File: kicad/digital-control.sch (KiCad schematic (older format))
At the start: 35 parts, among them J1 SWD, J2 EXTERNAL_OUT, J3 EXTERNAL_IN, J4 USB_OTG, U1 STM32F042FxP, U2 USBLC6-2

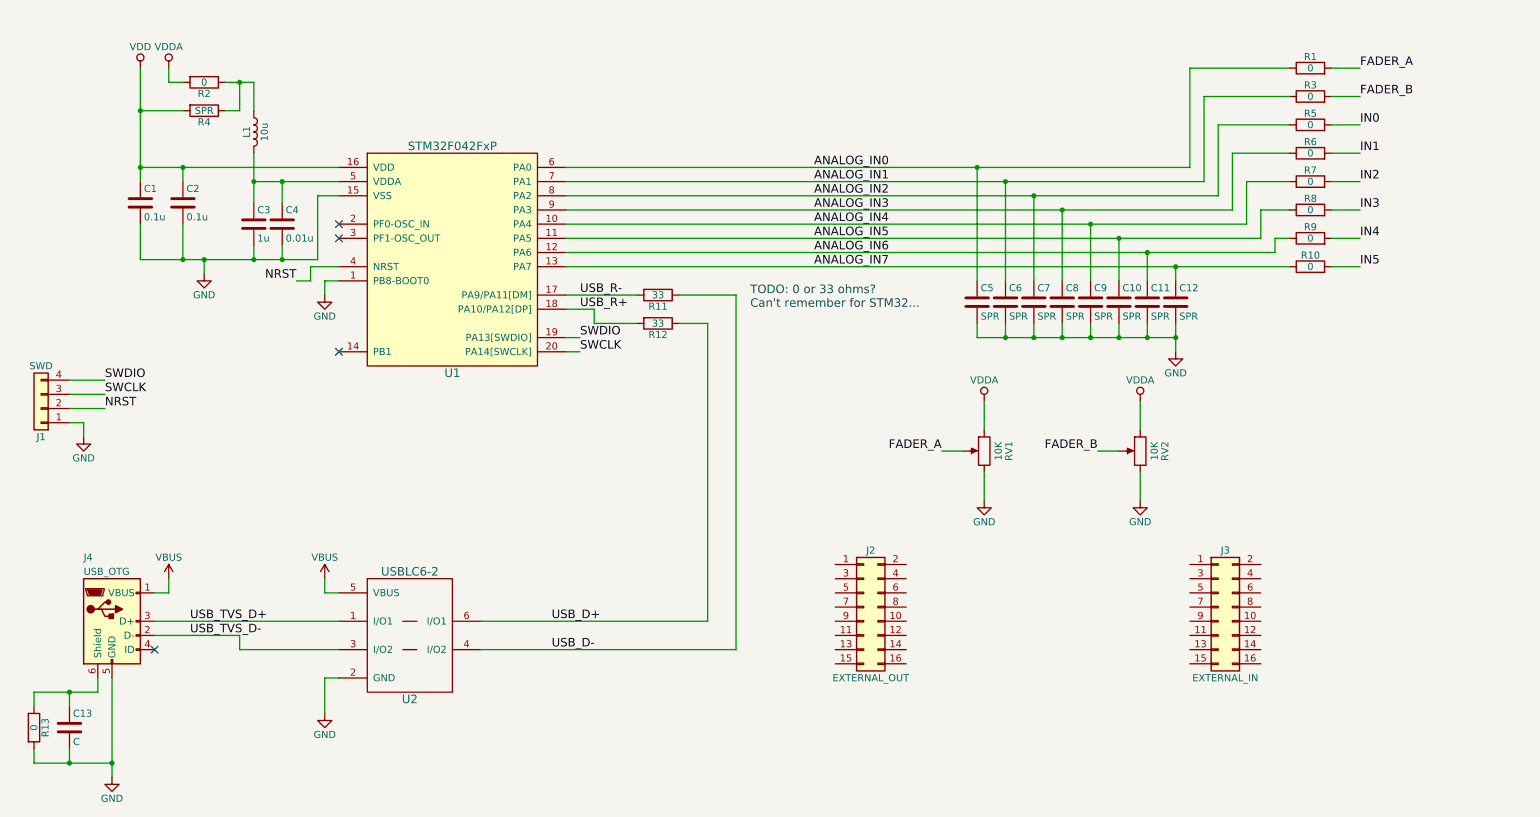
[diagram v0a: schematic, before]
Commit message: Finished initial part selection, built footprints
I'm not sure about my footprint selection for the expansion headers,
even though it is just a 0.1" header I want to be fairly exact about the
length the pins stick out and how close the female header is to the
edge, so that I can get a good distance between the two boards.
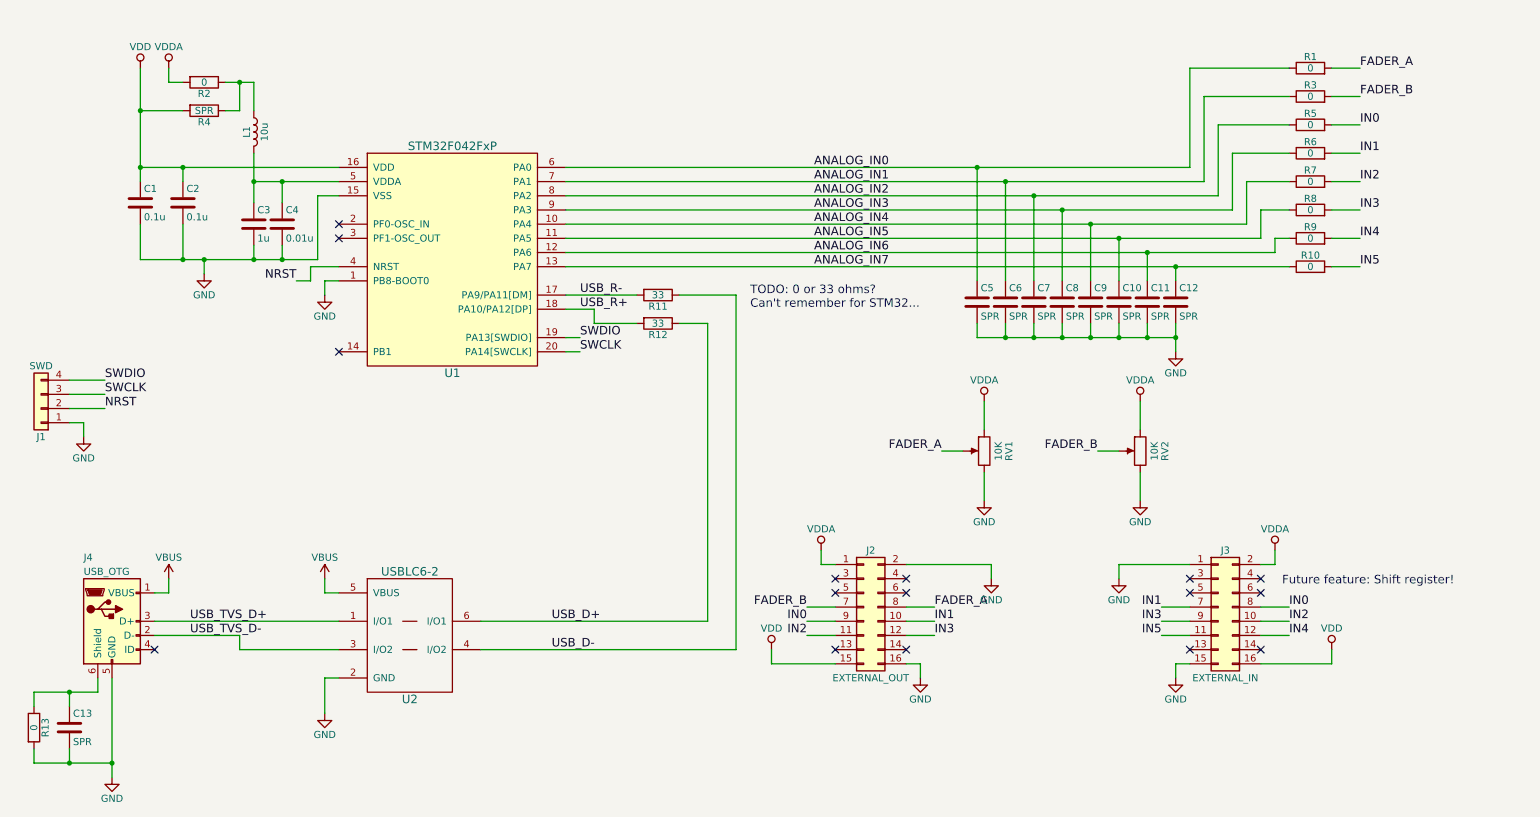
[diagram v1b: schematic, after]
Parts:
- C1, C2: footprint (none) -> Capacitors_SMD:C_0402; Part No. (none) -> 1276-1043-1-ND
- C10, C11, C12, C5, C6, C7, C8, C9: footprint (none) -> Capacitors_SMD:C_0402
- C13: value C -> SPR; footprint (none) -> Capacitors_SMD:C_0402
- C3: footprint (none) -> Capacitors_SMD:C_0603; Part No. (none) -> 1276-6524-1-ND
- C4: footprint (none) -> Capacitors_SMD:C_0402; Part No. (none) -> 399-1038-1-ND
- J1: footprint (none) -> midi-fader:JST-SH-4
- J2: footprint (none) -> Pin_Headers:Pin_Header_Angled_2x08_Pitch2.54mm
- J3: footprint (none) -> Socket_Strips:Socket_Strip_Angled_2x08_Pitch2.54mm
- J4: footprint (none) -> midi-fader:AMP-10104110-USB
- L1: footprint (none) -> Resistors_SMD:R_0805; Part No. (none) -> 587-2045-1-ND
- R1, R10, R11, R12, R13, R2, R3, R4, R5, R6, R7, R8, R9: footprint (none) -> Resistors_SMD:R_0402
- RV1, RV2: footprint (none) -> midi-fader:BOURNS_PTA60X3
- U1: footprint (none) -> Housings_SSOP:TSSOP-20_4.4x6.5mm_Pitch0.65mm
- U2: footprint (none) -> midi-fader:SOT-666
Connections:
- net FADER_A: now also J2.8 (Pin_8)
- net FADER_B: now also J2.7 (Pin_7)
- net GND: now also J2.16 (Pin_16), J2.2 (Pin_2), J3.1 (Pin_1), J3.15 (Pin_15)
- net IN0: now also J2.9 (Pin_9), J3.8 (Pin_8)
- net IN1: now also J2.10 (Pin_10), J3.7 (Pin_7)
- net IN2: now also J2.11 (Pin_11), J3.10 (Pin_10)
- net IN3: now also J2.12 (Pin_12), J3.9 (Pin_9)
- net IN4: now also J3.12 (Pin_12)
- net IN5: now also J3.11 (Pin_11)
- net VDD: now also J2.15 (Pin_15), J3.16 (Pin_16)
- net VDDA: now also J2.1 (Pin_1), J3.2 (Pin_2)
- no-connect marks 4 -> 16
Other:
- note added: "Future feature: Shift register!"

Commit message: Changed microcontroller to 32-LQFP variety
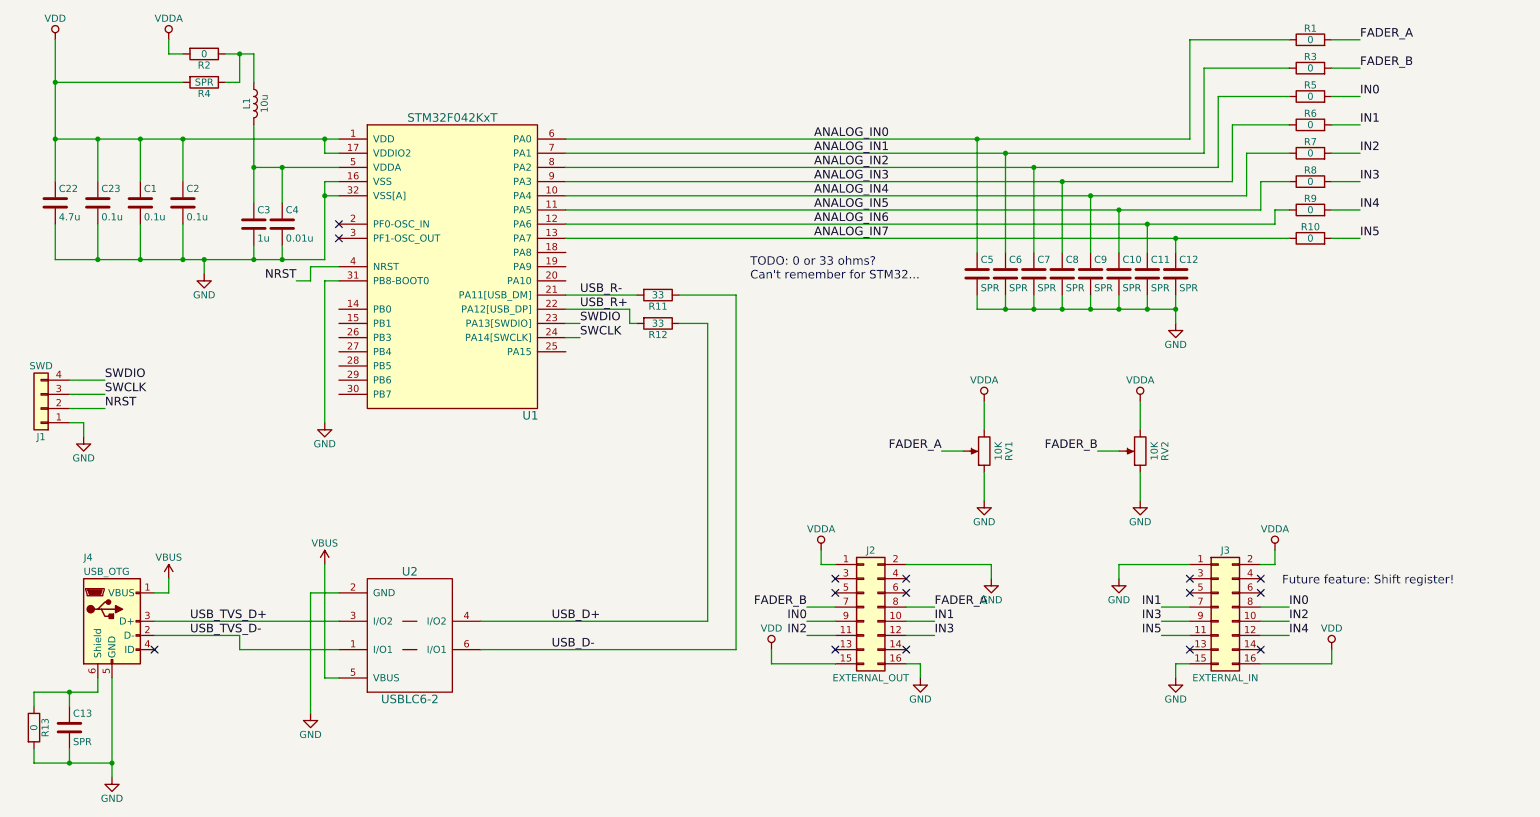
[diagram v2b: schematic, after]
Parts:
- removed U1: STM32F042FxP, Housings_SSOP:TSSOP-20_4.4x6.5mm_Pitch0.65mm, symbol STM32F042FxP
- added C22: 4.7u, Capacitors_SMD:C_0805, symbol C
- added C23: 0.1u, Capacitors_SMD:C_0402, symbol C
- added U1: STM32F042KxT, Housings_QFP:LQFP-32_7x7mm_Pitch0.8mm, symbol STM32F042KxT
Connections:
- net ANALOG_IN0: now also U1.6 (PA0)
- net ANALOG_IN1: now also U1.7 (PA1)
- net ANALOG_IN2: now also U1.8 (PA2)
- net ANALOG_IN3: now also U1.9 (PA3)
- net ANALOG_IN4: now also U1.10 (PA4)
- net ANALOG_IN5: now also U1.11 (PA5)
- net ANALOG_IN6: now also U1.12 (PA6)
- net ANALOG_IN7: now also U1.13 (PA7)
- net GND: now also RV1.1, RV2.1, C22.2, C23.2, U1.16 (VSS), U1.31 (PB8-BOOT0), U1.32 (VSS[A]); no longer RV1.3, RV2.3
- net NRST: now also U1.4 (NRST)
- net SWCLK: now also U1.24 (PA14[SWCLK])
- net SWDIO: now also U1.23 (PA13[SWDIO])
- net USB_D+: now also U2.4 (I/O2); no longer U2.6 (I/O1)
- net USB_D-: now also U2.6 (I/O1); no longer U2.4 (I/O2)
- net USB_R+: now also U1.22 (PA12[USB_DP])
- net USB_R-: now also U1.21 (PA11[USB_DM])
- net USB_TVS_D+: now also U2.3 (I/O2); no longer U2.1 (I/O1)
- net USB_TVS_D-: now also U2.1 (I/O1); no longer U2.3 (I/O2)
- net VDD: now also C22.1, C23.1, U1.1 (VDD), U1.17 (VDDIO2)
- net VDDA: now also RV1.3, RV2.3; no longer RV1.1, RV2.1
- net at C3.1, C4.1, L1.2: now also U1.5 (VDDA)
- no-connect marks 16 -> 15
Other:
- moved on the sheet: C10, C11, C12, C5, C6, C7, C8, C9, L1, R1, R10, R2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

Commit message: Completed initial placement
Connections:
- net GND: now also J3.16 (Pin_16), J3.2 (Pin_2); no longer J3.1 (Pin_1), J3.15 (Pin_15)
- net IN0: now also J3.7 (Pin_7); no longer J3.8 (Pin_8)
- net IN1: now also J3.8 (Pin_8); no longer J3.7 (Pin_7)
- net IN2: now also J3.9 (Pin_9); no longer J3.10 (Pin_10)
- net IN3: now also J3.10 (Pin_10); no longer J3.9 (Pin_9)
- net IN4: now also J3.11 (Pin_11); no longer J3.12 (Pin_12)
- net IN5: now also J3.12 (Pin_12); no longer J3.11 (Pin_11)
- net VDD: now also J3.15 (Pin_15); no longer J3.16 (Pin_16)
- net VDDA: now also J3.1 (Pin_1); no longer J3.2 (Pin_2)
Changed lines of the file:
@@
 L Conn_02x08_Odd_Even J3
 U 1 1 5B3D8AF7
-P 9100 4800
-F 0 "J3" H 9150 5200 50  0000 C CNN
-F 1 "EXTERNAL_IN" H 9150 4300 50  0000 C CNN
-F 2 "Socket_Strips:Socket_Strip_Angled_2x08_Pitch2.54mm" H 9100 4800 50  0001 C CNN
-F 3 "" H 9100 4800 50  0001 C CNN
-F 4 "S5561-ND" H 9100 4800 60  0001 C CNN "Part No."
-	1    9100 4800
-	1    0    0    -1
+P 9200 4800
+F 0 "J3" H 9250 5200 50  0000 C CNN
+F 1 "EXTERNAL_IN" H 9250 4300 50  0000 C CNN
+F 2 "Socket_Strips:Socket_Strip_Angled_2x08_Pitch2.54mm" H 9200 4800 50  0001 C CNN
+F 3 "" H 9200 4800 50  0001 C CNN
+F 4 "S5561-ND" H 9200 4800 60  0001 C CNN "Part No."
+	1    9200 4800
+	-1   0    0    -1
 $EndComp
 $Comp

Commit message: Initial routing complete
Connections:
- net VDD: now also J2.1 (Pin_1), J3.1 (Pin_1); no longer J2.15 (Pin_15), J3.15 (Pin_15)
- net VDDA: now also J2.15 (Pin_15), J3.15 (Pin_15); no longer J2.1 (Pin_1), J3.1 (Pin_1)
- net CHSGND: now reaches C13.1, J4.6 (Shield), R13.1
- net VDDA_UC: now reaches C3.1, C4.1, L1.2, U1.5 (VDDA)
- net VDDA_UC_PREFILT: now reaches L1.1, R2.1, R4.1
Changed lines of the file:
@@
 L VDDA #PWR017
 U 1 1 5B3E32A0
-P 6300 4400
-F 0 "#PWR017" H 6300 4250 50  0001 C CNN
-F 1 "VDDA" H 6300 4550 50  0000 C CNN
-F 2 "" H 6300 4400 50  0001 C CNN
-F 3 "" H 6300 4400 50  0001 C CNN
-	1    6300 4400
+P 5950 5100
+F 0 "#PWR017" H 5950 4950 50  0001 C CNN
+F 1 "VDDA" H 5950 5250 50  0000 C CNN
+F 2 "" H 5950 5100 50  0001 C CNN
+F 3 "" H 5950 5100 50  0001 C CNN
+	1    5950 5100
 	1    0    0    -1
 $EndComp
@@
 L VDDA #PWR018
 U 1 1 5B3E334F
-P 9500 4400
-F 0 "#PWR018" H 9500 4250 50  0001 C CNN
-F 1 "VDDA" H 9500 4550 50  0000 C CNN
-F 2 "" H 9500 4400 50  0001 C CNN
-F 3 "" H 9500 4400 50  0001 C CNN
-	1    9500 4400
+P 9900 5100
+F 0 "#PWR018" H 9900 4950 50  0001 C CNN
+F 1 "VDDA" H 9900 5250 50  0000 C CNN
+F 2 "" H 9900 5100 50  0001 C CNN
+F 3 "" H 9900 5100 50  0001 C CNN
+	1    9900 5100
 	1    0    0    -1
 $EndComp
@@
 L VDD #PWR019
 U 1 1 5B3E3AEB
-P 5950 5100
-F 0 "#PWR019" H 5950 4950 50  0001 C CNN
-F 1 "VDD" H 5950 5250 50  0000 C CNN
-F 2 "" H 5950 5100 50  0001 C CNN
-F 3 "" H 5950 5100 50  0001 C CNN
-	1    5950 5100
+P 6300 4400
+F 0 "#PWR019" H 6300 4250 50  0001 C CNN
+F 1 "VDD" H 6300 4550 50  0000 C CNN
+F 2 "" H 6300 4400 50  0001 C CNN
+F 3 "" H 6300 4400 50  0001 C CNN
+	1    6300 4400
 	1    0    0    -1
 $EndComp
@@
 L VDD #PWR020
 U 1 1 5B3E3D26
-P 9900 5100
-F 0 "#PWR020" H 9900 4950 50  0001 C CNN
-F 1 "VDD" H 9900 5250 50  0000 C CNN
-F 2 "" H 9900 5100 50  0001 C CNN
-F 3 "" H 9900 5100 50  0001 C CNN
-	1    9900 5100
+P 9500 4400
+F 0 "#PWR020" H 9500 4250 50  0001 C CNN
+F 1 "VDD" H 9500 4550 50  0000 C CNN
+F 2 "" H 9500 4400 50  0001 C CNN
+F 3 "" H 9500 4400 50  0001 C CNN
+	1    9500 4400
 	1    0    0    -1
 $EndComp
@@
 	1500 2100 1500 2350
 Connection ~ 1500 2350
+Text Label 750  5400 0    60   ~ 0
+CHSGND
+Text Label 2400 1700 0    60   ~ 0
+VDDA_UC
+Text Label 2150 900  0    60   ~ 0
+VDDA_UC_PREFILT
 $EndSCHEMATC

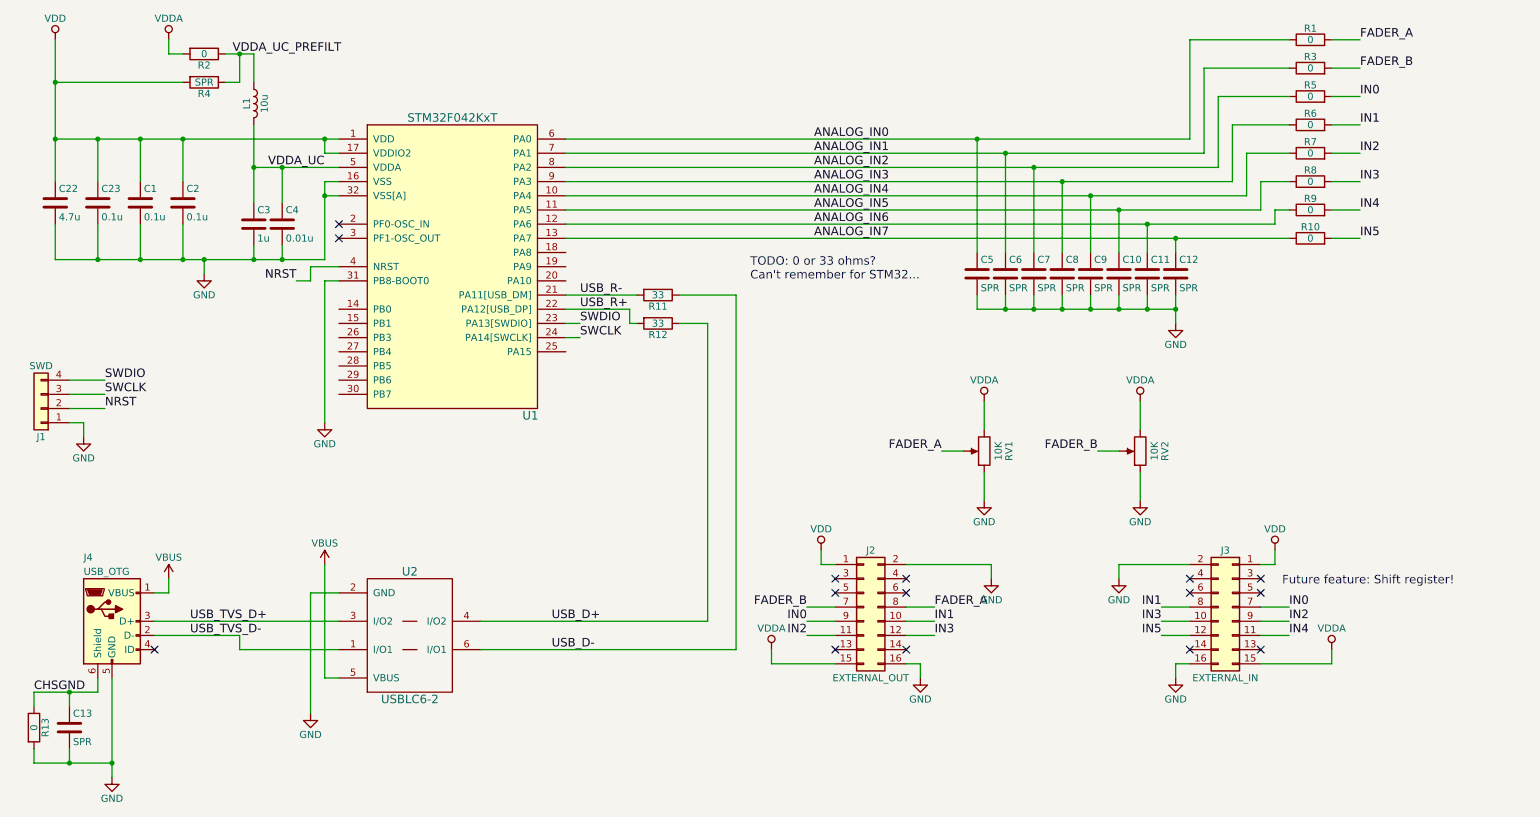
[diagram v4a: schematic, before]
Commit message: Restructured schematic to have a separate input page
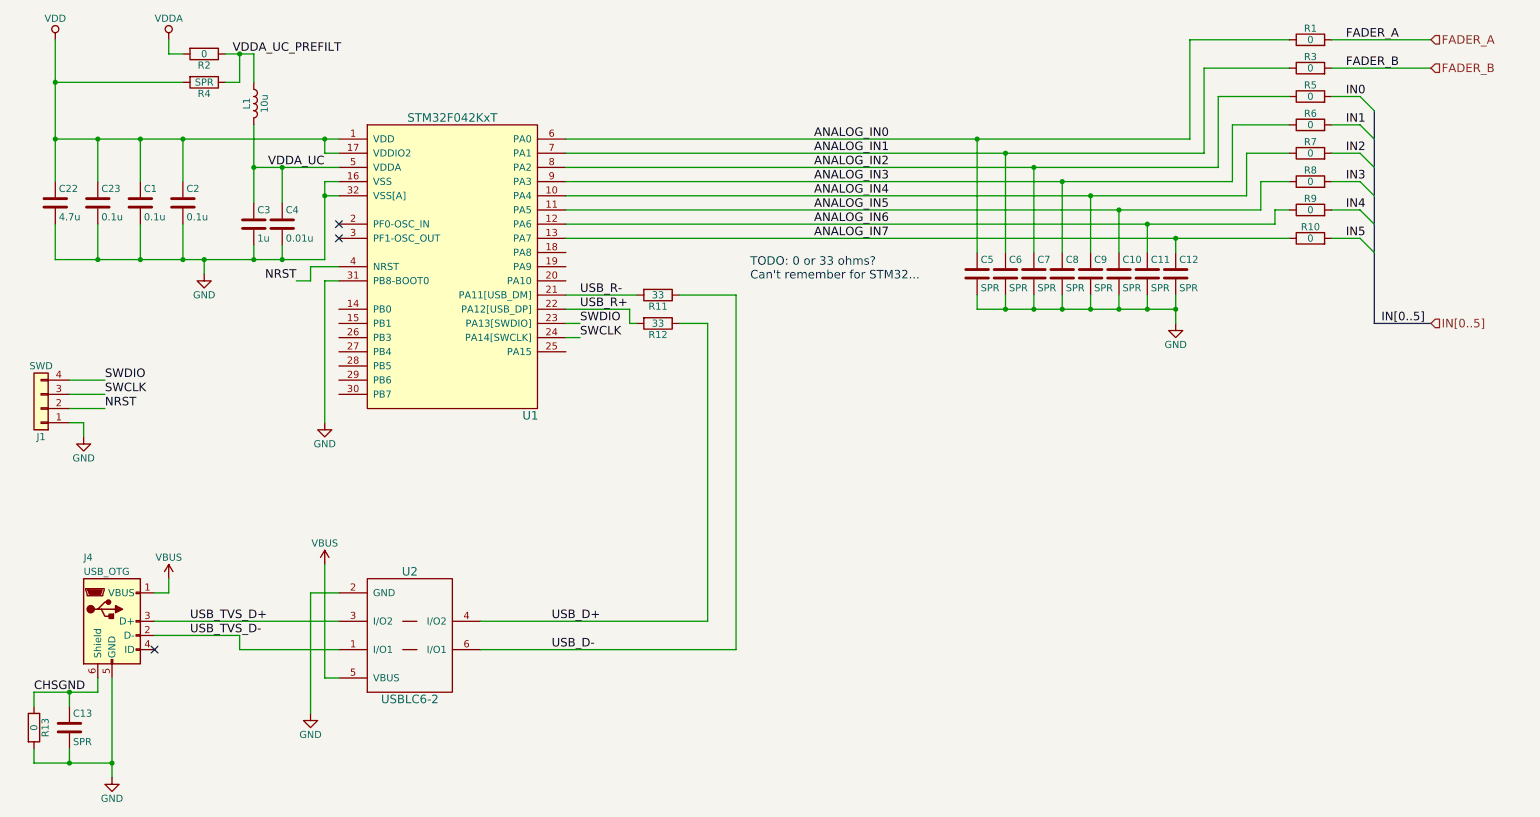
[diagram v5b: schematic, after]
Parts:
- removed J2: EXTERNAL_OUT, Pin_Headers:Pin_Header_Angled_2x08_Pitch2.54mm, symbol Conn_02x08_Odd_Even
- removed J3: EXTERNAL_IN, Socket_Strips:Socket_Strip_Angled_2x08_Pitch2.54mm, symbol Conn_02x08_Odd_Even
- removed RV1, RV2: 10K, midi-fader:BOURNS_PTA60X3, symbol POT
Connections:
- no-connect marks 15 -> 3
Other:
- note removed: "Future feature: Shift register!"
